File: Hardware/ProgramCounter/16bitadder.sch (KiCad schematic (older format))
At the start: 4 parts

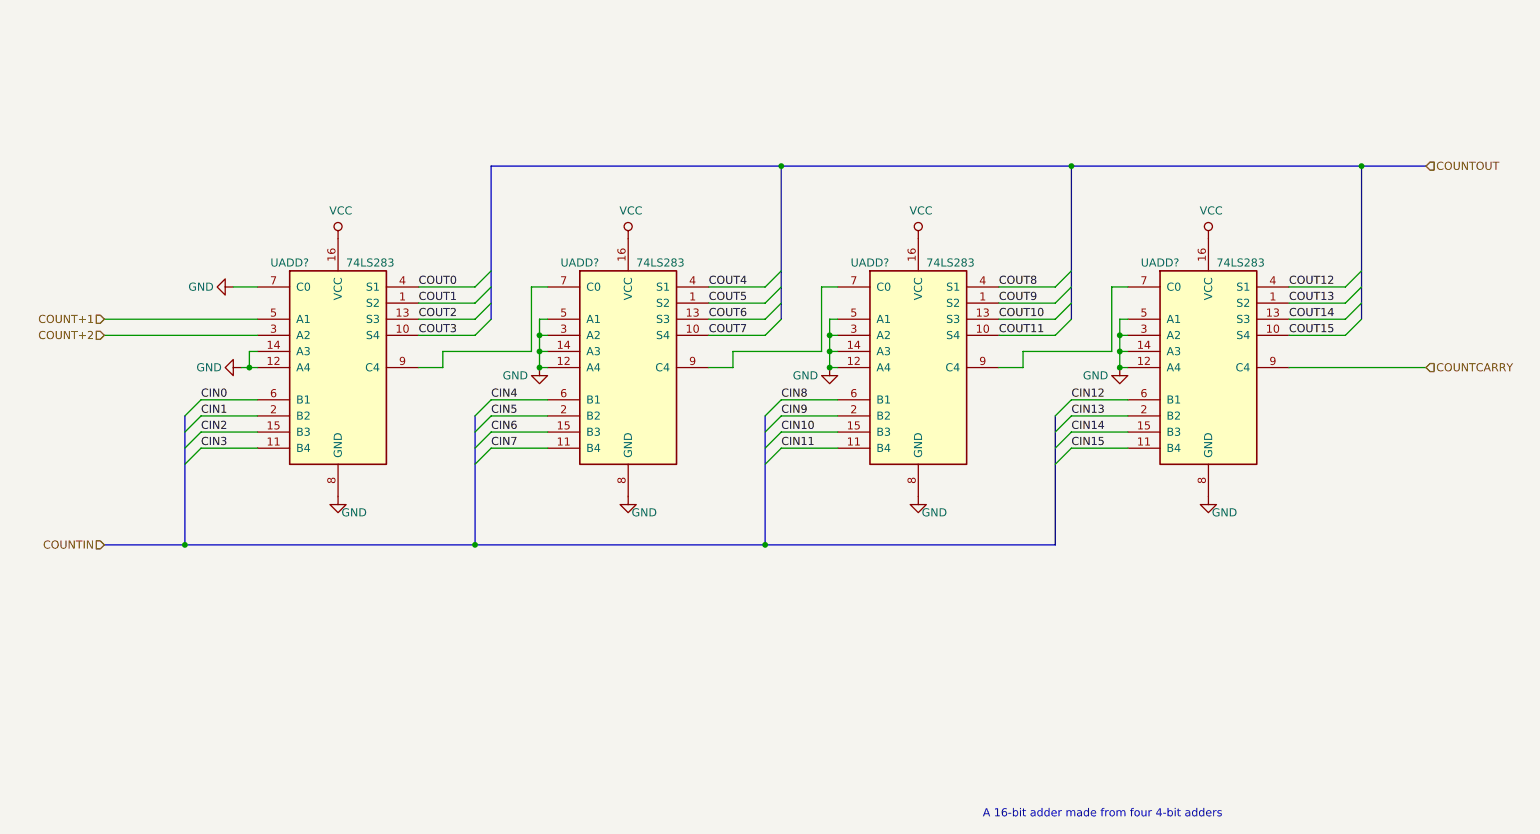
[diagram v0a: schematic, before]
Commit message: Started to make Schematic for the Program Counter.
TODO: Complete schematic, buy parts, layout PCB, solder PCB.

Then logically test the PCB using a digital oscilloscope.

Then repeat for 4-5 other PCBs.
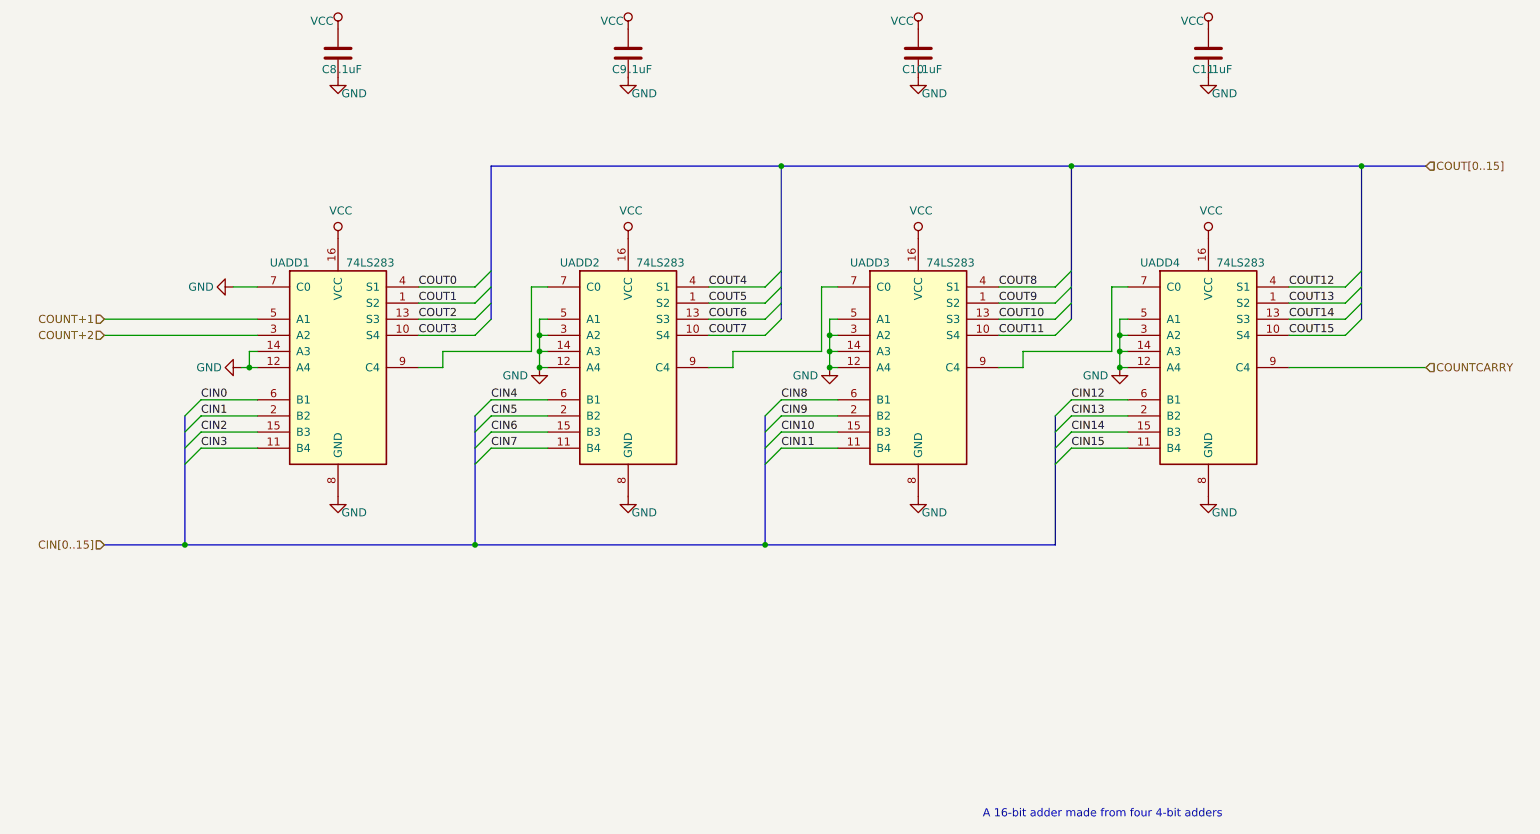
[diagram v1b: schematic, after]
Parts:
- added C10, C11, C8, C9: .1uF, symbol Device:C
- UADD1, UADD2, UADD3, UADD4: renamed from UADD?; footprint (none) -> Package_SO:TSSOP-16_4.4x5mm_P0.65mm
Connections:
- net GND: now also C10.2, C11.2, C8.2, C9.2
- net VCC: now also C10.1, C11.1, C8.1, C9.1

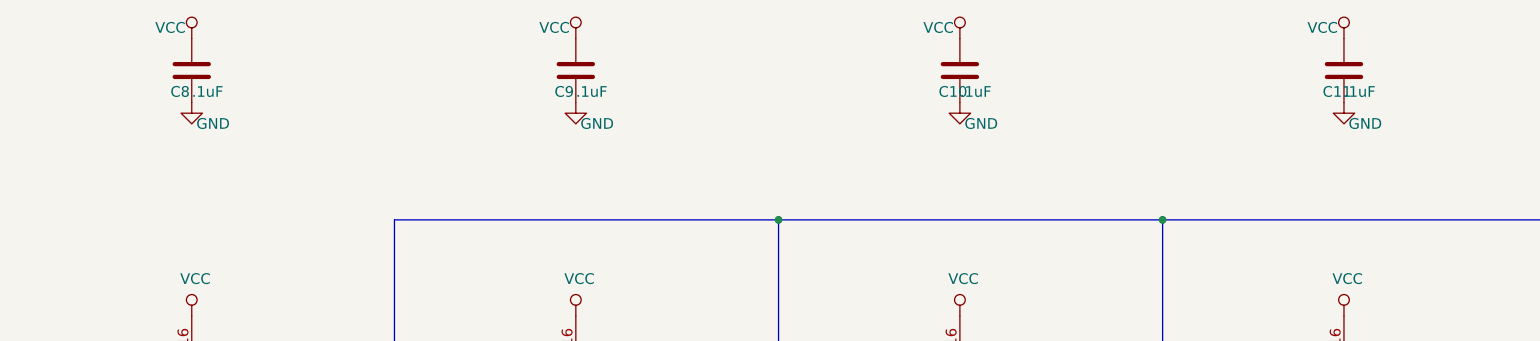
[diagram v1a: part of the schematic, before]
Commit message: PC PCB Progress
Mostly done with schematic for the Program Counter. I'll order parts soon and start on the PCB design next. It'll be my first four layer board!

Based on what I've seen so far, CMOS seems to be more prevalent than TTL, so I'll make this computer out of CMOS.
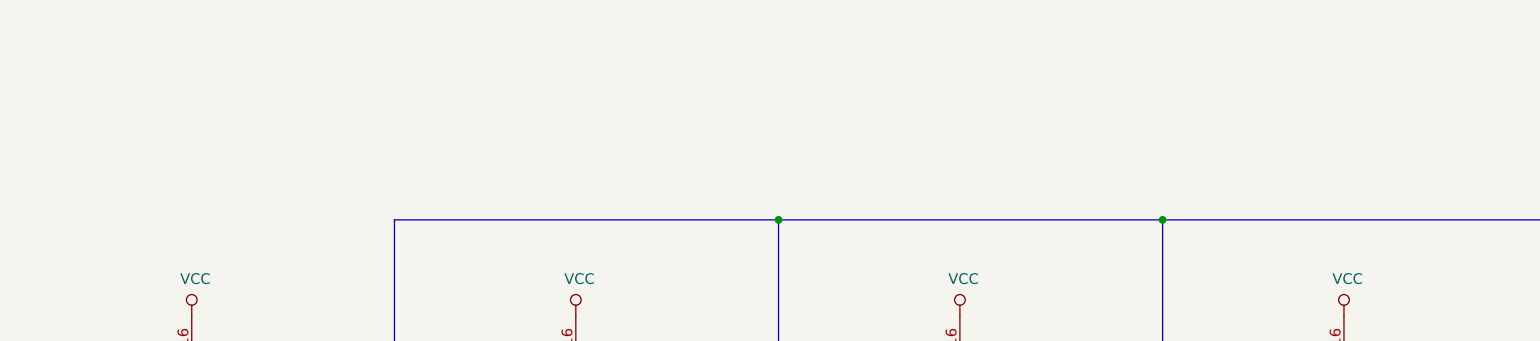
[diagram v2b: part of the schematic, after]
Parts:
- removed C10, C11, C8, C9: .1uF, symbol Device:C
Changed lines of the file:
@@
 Wire Wire Line
 	9750 3850 8900 3850
-$Comp
-L power:VCC #PWR?
-U 1 1 62A2A21D
-P 3000 1750
-AR Path="/62A2A21D" Ref="#PWR?"  Part="1"
-AR Path="/6282316B/62A2A21D" Ref="#PWR0154"  Part="1"
-F 0 "#PWR0154" H 3000 1600 50  0001 C CNN
-F 1 "VCC" H 2900 1800 50  0000 C CNN
-F 2 "" H 3000 1750 50  0001 C CNN
-F 3 "" H 3000 1750 50  0001 C CNN
-	1    3000 1750
-	1    0    0    -1
-$EndComp
-$Comp
-L Device:C C?
-U 1 1 62A2A223
-P 3000 1900
-AR Path="/62A2A223" Ref="C?"  Part="1"
-AR Path="/6282316B/62A2A223" Ref="C8"  Part="1"
-F 0 "C8" H 2900 1800 50  0000 L CNN
-F 1 ".1uF" H 3000 1800 50  0000 L CNN
-F 2 "" H 3038 1750 50  0001 C CNN
-F 3 "~" H 3000 1900 50  0001 C CNN
-	1    3000 1900
-	1    0    0    -1
-$EndComp
-$Comp
-L power:GND #PWR?
-U 1 1 62A2A229
-P 3000 2050
-AR Path="/62A2A229" Ref="#PWR?"  Part="1"
-AR Path="/6282316B/62A2A229" Ref="#PWR0155"  Part="1"
-F 0 "#PWR0155" H 3000 1800 50  0001 C CNN
-F 1 "GND" H 3100 1950 50  0000 C CNN
-F 2 "" H 3000 2050 50  0001 C CNN
-F 3 "" H 3000 2050 50  0001 C CNN
-	1    3000 2050
-	1    0    0    -1
-$EndComp
-$Comp
-L power:VCC #PWR?
-U 1 1 62A2C95E
-P 4800 1750
-AR Path="/62A2C95E" Ref="#PWR?"  Part="1"
-AR Path="/6282316B/62A2C95E" Ref="#PWR0156"  Part="1"
-F 0 "#PWR0156" H 4800 1600 50  0001 C CNN
-F 1 "VCC" H 4700 1800 50  0000 C CNN
-F 2 "" H 4800 1750 50  0001 C CNN
-F 3 "" H 4800 1750 50  0001 C CNN
-	1    4800 1750
-	1    0    0    -1
-$EndComp
-$Comp
-L Device:C C?
-U 1 1 62A2C964
-P 4800 1900
-AR Path="/62A2C964" Ref="C?"  Part="1"
-AR Path="/6282316B/62A2C964" Ref="C9"  Part="1"
-F 0 "C9" H 4700 1800 50  0000 L CNN
-F 1 ".1uF" H 4800 1800 50  0000 L CNN
-F 2 "" H 4838 1750 50  0001 C CNN
-F 3 "~" H 4800 1900 50  0001 C CNN
-	1    4800 1900
-	1    0    0    -1
-$EndComp
-$Comp
-L power:GND #PWR?
-U 1 1 62A2C96A
-P 4800 2050
-AR Path="/62A2C96A" Ref="#PWR?"  Part="1"
-AR Path="/6282316B/62A2C96A" Ref="#PWR0157"  Part="1"
-F 0 "#PWR0157" H 4800 1800 50  0001 C CNN
-F 1 "GND" H 4900 1950 50  0000 C CNN
-F 2 "" H 4800 2050 50  0001 C CNN
-F 3 "" H 4800 2050 50  0001 C CNN
-	1    4800 2050
-	1    0    0    -1
-$EndComp
-$Comp
-L power:VCC #PWR?
-U 1 1 62A2EF78
-P 6600 1750
-AR Path="/62A2EF78" Ref="#PWR?"  Part="1"
-AR Path="/6282316B/62A2EF78" Ref="#PWR0158"  Part="1"
-F 0 "#PWR0158" H 6600 1600 50  0001 C CNN
-F 1 "VCC" H 6500 1800 50  0000 C CNN
-F 2 "" H 6600 1750 50  0001 C CNN
-F 3 "" H 6600 1750 50  0001 C CNN
-	1    6600 1750
-	1    0    0    -1
-$EndComp
-$Comp
-L Device:C C?
-U 1 1 62A2EF7E
-P 6600 1900
-AR Path="/62A2EF7E" Ref="C?"  Part="1"
-AR Path="/6282316B/62A2EF7E" Ref="C10"  Part="1"
-F 0 "C10" H 6500 1800 50  0000 L CNN
-F 1 ".1uF" H 6600 1800 50  0000 L CNN
-F 2 "" H 6638 1750 50  0001 C CNN
-F 3 "~" H 6600 1900 50  0001 C CNN
-	1    6600 1900
-	1    0    0    -1
-$EndComp
-$Comp
-L power:GND #PWR?
-U 1 1 62A2EF84
-P 6600 2050
-AR Path="/62A2EF84" Ref="#PWR?"  Part="1"
-AR Path="/6282316B/62A2EF84" Ref="#PWR0159"  Part="1"
-F 0 "#PWR0159" H 6600 1800 50  0001 C CNN
-F 1 "GND" H 6700 1950 50  0000 C CNN
-F 2 "" H 6600 2050 50  0001 C CNN
-F 3 "" H 6600 2050 50  0001 C CNN
-	1    6600 2050
-	1    0    0    -1
-$EndComp
-$Comp
-L power:VCC #PWR?
-U 1 1 62A31A1A
-P 8400 1750
-AR Path="/62A31A1A" Ref="#PWR?"  Part="1"
-AR Path="/6282316B/62A31A1A" Ref="#PWR0160"  Part="1"
-F 0 "#PWR0160" H 8400 1600 50  0001 C CNN
-F 1 "VCC" H 8300 1800 50  0000 C CNN
-F 2 "" H 8400 1750 50  0001 C CNN
-F 3 "" H 8400 1750 50  0001 C CNN
-	1    8400 1750
-	1    0    0    -1
-$EndComp
-$Comp
-L Device:C C?
-U 1 1 62A31A20
-P 8400 1900
-AR Path="/62A31A20" Ref="C?"  Part="1"
-AR Path="/6282316B/62A31A20" Ref="C11"  Part="1"
-F 0 "C11" H 8300 1800 50  0000 L CNN
-F 1 ".1uF" H 8400 1800 50  0000 L CNN
-F 2 "" H 8438 1750 50  0001 C CNN
-F 3 "~" H 8400 1900 50  0001 C CNN
-	1    8400 1900
-	1    0    0    -1
-$EndComp
-$Comp
-L power:GND #PWR?
-U 1 1 62A31A26
-P 8400 2050
-AR Path="/62A31A26" Ref="#PWR?"  Part="1"
-AR Path="/6282316B/62A31A26" Ref="#PWR0161"  Part="1"
-F 0 "#PWR0161" H 8400 1800 50  0001 C CNN
-F 1 "GND" H 8500 1950 50  0000 C CNN
-F 2 "" H 8400 2050 50  0001 C CNN
-F 3 "" H 8400 2050 50  0001 C CNN
-	1    8400 2050
-	1    0    0    -1
-$EndComp
 Wire Bus Line
 	3850 4150 3850 4950

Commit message: PC Schematic
Mostly finished Program Counter schematic. I'm basing the hardware largely off of TI's new HCS family of SN74HCS chips.
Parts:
- UADD1, UADD2, UADD3, UADD4: footprint Package_SO:TSSOP-16_4.4x5mm_P0.65mm -> aFootprint:R-PDSO-G16
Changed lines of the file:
@@
 F 0 "UADD1" H 2700 4500 50  0000 C CNN
 F 1 "74LS283" H 3200 4500 50  0000 C CNN
-F 2 "Package_SO:TSSOP-16_4.4x5mm_P0.65mm" H 3000 3850 50  0001 C CNN
+F 2 "aFootprint:R-PDSO-G16" H 3000 3850 50  0001 C CNN
 F 3 "http://www.ti.com/lit/gpn/sn74LS283" H 3000 3850 50  0001 C CNN
 	1    3000 3850
@@
 F 0 "UADD2" H 4500 4500 50  0000 C CNN
 F 1 "74LS283" H 5000 4500 50  0000 C CNN
-F 2 "Package_SO:TSSOP-16_4.4x5mm_P0.65mm" H 4800 3850 50  0001 C CNN
+F 2 "aFootprint:R-PDSO-G16" H 4800 3850 50  0001 C CNN
 F 3 "http://www.ti.com/lit/gpn/sn74LS283" H 4800 3850 50  0001 C CNN
 	1    4800 3850
@@
 F 0 "UADD3" H 6300 4500 50  0000 C CNN
 F 1 "74LS283" H 6800 4500 50  0000 C CNN
-F 2 "Package_SO:TSSOP-16_4.4x5mm_P0.65mm" H 6600 3850 50  0001 C CNN
+F 2 "aFootprint:R-PDSO-G16" H 6600 3850 50  0001 C CNN
 F 3 "http://www.ti.com/lit/gpn/sn74LS283" H 6600 3850 50  0001 C CNN
 	1    6600 3850
@@
 F 0 "UADD4" H 8100 4500 50  0000 C CNN
 F 1 "74LS283" H 8600 4500 50  0000 C CNN
-F 2 "Package_SO:TSSOP-16_4.4x5mm_P0.65mm" H 8400 3850 50  0001 C CNN
+F 2 "aFootprint:R-PDSO-G16" H 8400 3850 50  0001 C CNN
 F 3 "http://www.ti.com/lit/gpn/sn74LS283" H 8400 3850 50  0001 C CNN
 	1    8400 3850

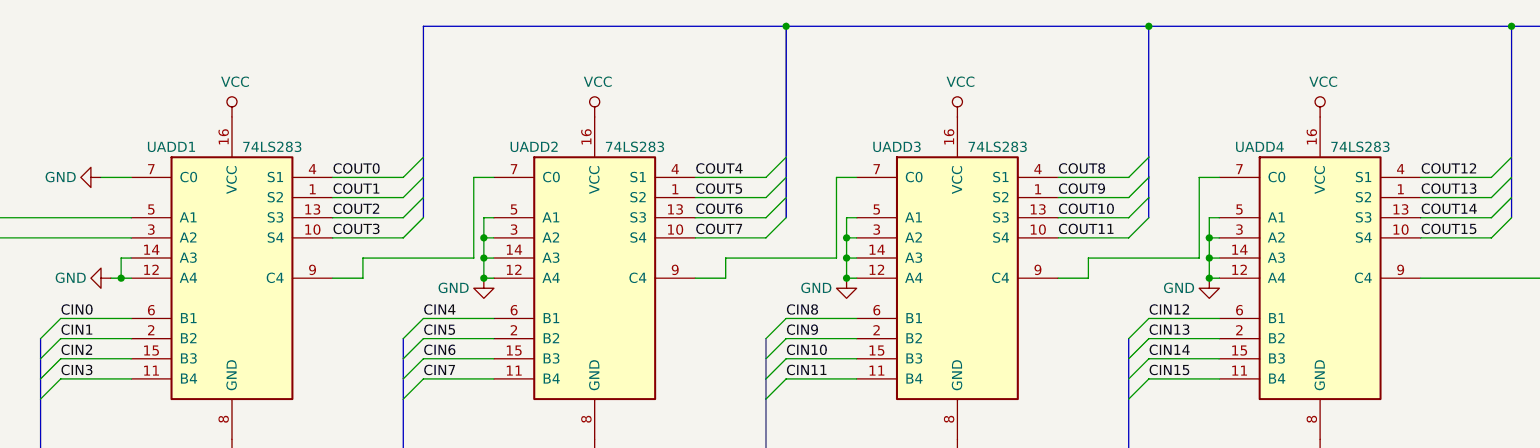
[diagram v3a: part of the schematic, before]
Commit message: PC Board
Mostly done. Going to move top half down.
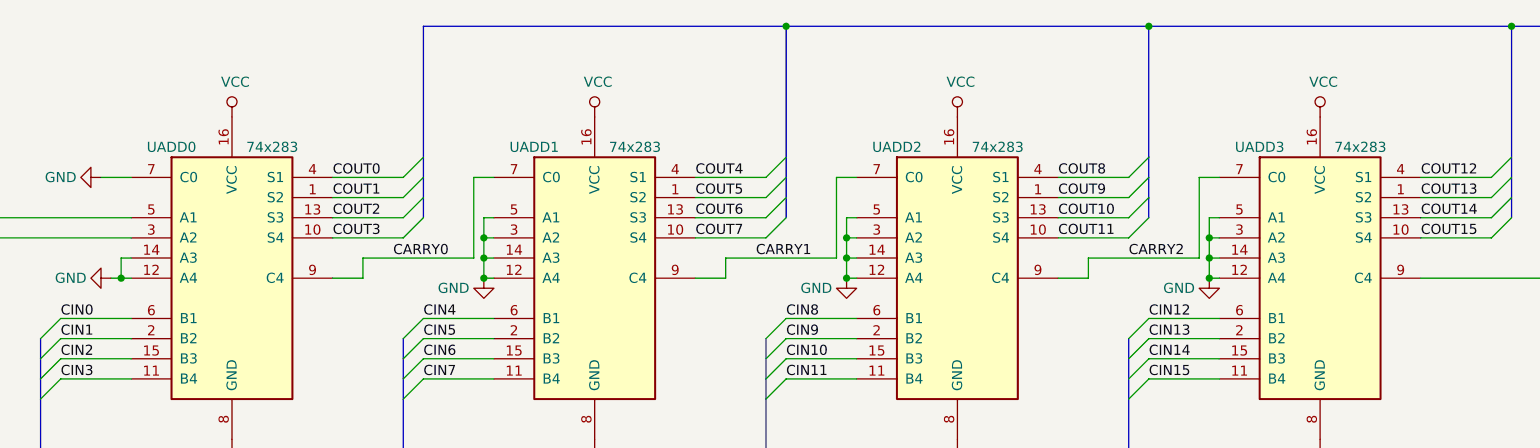
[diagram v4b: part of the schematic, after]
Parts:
- UADD0: renamed from UADD1; value 74LS283 -> 74x283
- UADD1: renamed from UADD2; value 74LS283 -> 74x283
- UADD2: renamed from UADD3; value 74LS283 -> 74x283
- UADD3: renamed from UADD4; value 74LS283 -> 74x283
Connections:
- net CARRY0: now reaches UADD0.9 (C4), UADD1.7 (C0)
- net CARRY1: now reaches UADD1.9 (C4), UADD2.7 (C0)
- net CARRY2: now reaches UADD2.9 (C4), UADD3.7 (C0)
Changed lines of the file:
@@
 P 3000 3850
 AR Path="/628499F1" Ref="UADD?"  Part="1"
-AR Path="/6282316B/628499F1" Ref="UADD1"  Part="1"
-F 0 "UADD1" H 2700 4500 50  0000 C CNN
-F 1 "74LS283" H 3200 4500 50  0000 C CNN
+AR Path="/6282316B/628499F1" Ref="UADD0"  Part="1"
+F 0 "UADD0" H 2700 4500 50  0000 C CNN
+F 1 "74x283" H 3200 4500 50  0000 C CNN
 F 2 "aFootprint:R-PDSO-G16" H 3000 3850 50  0001 C CNN
 F 3 "http://www.ti.com/lit/gpn/sn74LS283" H 3000 3850 50  0001 C CNN
@@
 P 4800 3850
 AR Path="/62849A0B" Ref="UADD?"  Part="1"
-AR Path="/6282316B/62849A0B" Ref="UADD2"  Part="1"
-F 0 "UADD2" H 4500 4500 50  0000 C CNN
-F 1 "74LS283" H 5000 4500 50  0000 C CNN
+AR Path="/6282316B/62849A0B" Ref="UADD1"  Part="1"
+F 0 "UADD1" H 4500 4500 50  0000 C CNN
+F 1 "74x283" H 5000 4500 50  0000 C CNN
 F 2 "aFootprint:R-PDSO-G16" H 4800 3850 50  0001 C CNN
 F 3 "http://www.ti.com/lit/gpn/sn74LS283" H 4800 3850 50  0001 C CNN
@@
 P 6600 3850
 AR Path="/62849A5C" Ref="UADD?"  Part="1"
-AR Path="/6282316B/62849A5C" Ref="UADD3"  Part="1"
-F 0 "UADD3" H 6300 4500 50  0000 C CNN
-F 1 "74LS283" H 6800 4500 50  0000 C CNN
+AR Path="/6282316B/62849A5C" Ref="UADD2"  Part="1"
+F 0 "UADD2" H 6300 4500 50  0000 C CNN
+F 1 "74x283" H 6800 4500 50  0000 C CNN
 F 2 "aFootprint:R-PDSO-G16" H 6600 3850 50  0001 C CNN
 F 3 "http://www.ti.com/lit/gpn/sn74LS283" H 6600 3850 50  0001 C CNN
@@
 P 8400 3850
 AR Path="/62863A6B" Ref="UADD?"  Part="1"
-AR Path="/6282316B/62863A6B" Ref="UADD4"  Part="1"
-F 0 "UADD4" H 8100 4500 50  0000 C CNN
-F 1 "74LS283" H 8600 4500 50  0000 C CNN
+AR Path="/6282316B/62863A6B" Ref="UADD3"  Part="1"
+F 0 "UADD3" H 8100 4500 50  0000 C CNN
+F 1 "74x283" H 8600 4500 50  0000 C CNN
 F 2 "aFootprint:R-PDSO-G16" H 8400 3850 50  0001 C CNN
 F 3 "http://www.ti.com/lit/gpn/sn74LS283" H 8400 3850 50  0001 C CNN
@@
 Wire Wire Line
 	9750 3850 8900 3850
+Text Label 3800 3750 0    50   ~ 0
+CARRY0
+Text Label 5600 3750 0    50   ~ 0
+CARRY1
+Text Label 7450 3750 0    50   ~ 0
+CARRY2
 Wire Bus Line
 	3850 4150 3850 4950
